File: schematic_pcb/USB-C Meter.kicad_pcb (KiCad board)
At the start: 4 copper layers, 51.5 x 45 mm, 68 parts, among them J1 USB-C 12P, J2 USB-C 12P, J3 Generic IN, J4 Generic OUT, J5 USB_B_Micro, J6 Display, J7 U.FL, J8 UART, U1 MP4560DN, U2 ME6211C33, U3 TPS2115, U4 ESP32-C3FH4, U6 INA228, Y1 40MHz

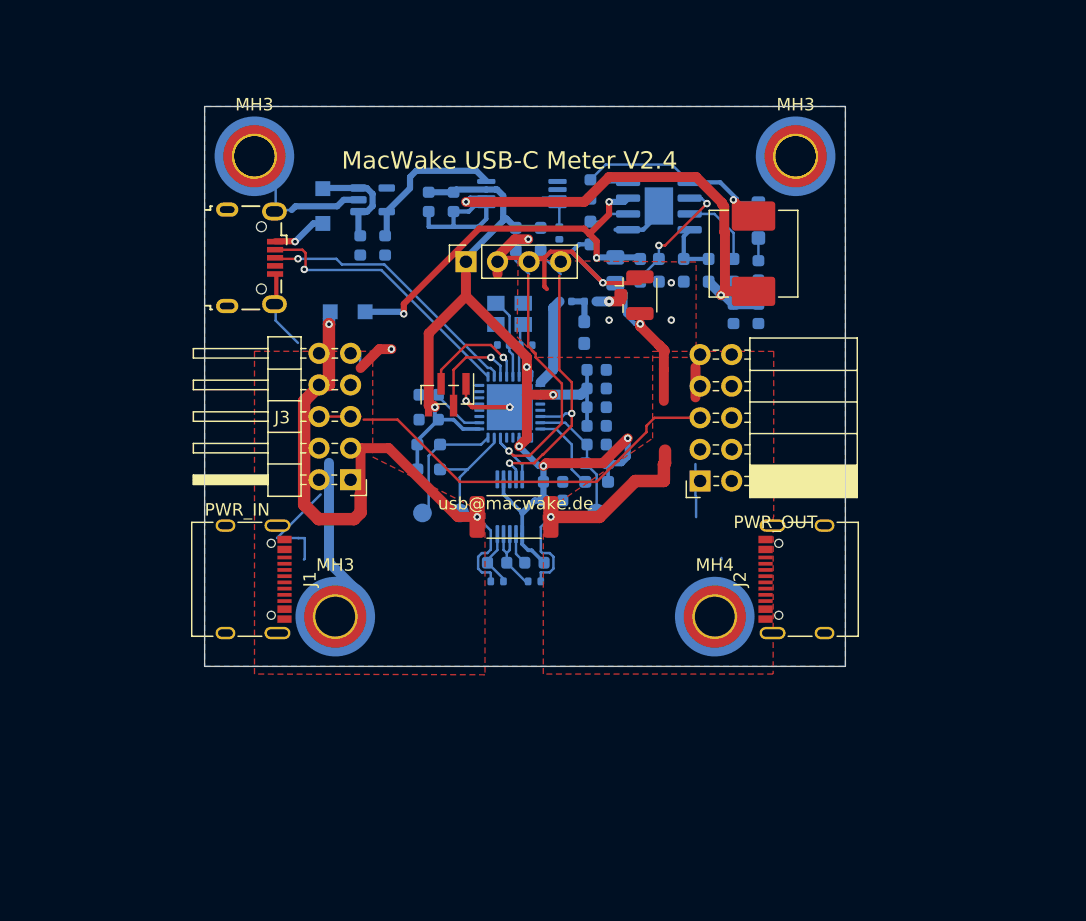
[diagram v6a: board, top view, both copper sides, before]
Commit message: fix: rf antenna pcb design, added reset tactile switch
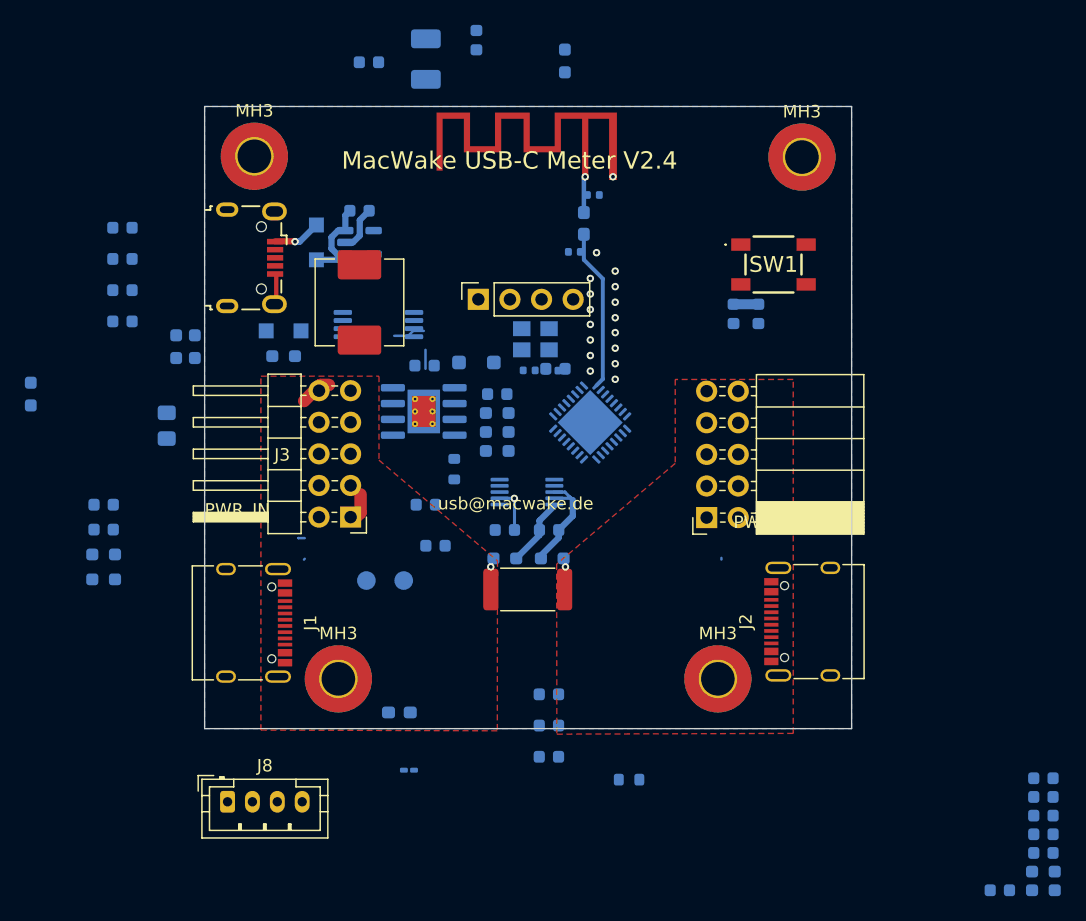
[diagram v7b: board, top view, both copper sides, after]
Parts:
- removed ? (x2): , 
- removed J7: U.FL, Connector_Coaxial:U.FL_Hirose_U.FL-R-SMT-1_Vertical
- removed MH4: MountingHole_3.2mm_M3_Pad_TopBottom, MountingHole:MountingHole_3.2mm_M3_Pad_TopBottom
- removed TP3: Reset, TestPoint:TestPoint_Pad_D1.5mm
- added AE1: Antenna_Shield, schematic_pcb:ESPRESSIF_ESP32_MIFA_2.4GHz_Right, F.Cu at (79.8, 30.6)
- added C2: 10µ, Capacitor_SMD:C_0603_1608Metric, B.Cu at (86.2, 72.2)
- added C27: .1µ, Capacitor_SMD:C_0603_1608Metric, B.Cu at (86.2, 77.3)
- added C28: .1µ, Capacitor_SMD:C_0603_1608Metric, B.Cu at (76.3, 57.0)
- added C29: 1µ, Capacitor_SMD:C_0603_1608Metric, B.Cu at (77.1, 60.3)
- added C3: 0.1µ, Capacitor_SMD:C_0603_1608Metric, B.Cu at (86.2, 74.8)
- added C30: .1µ, Capacitor_SMD:C_0603_1608Metric, B.Cu at (51.9, 37.3)
- added C31: .1µ, Capacitor_SMD:C_0603_1608Metric, B.Cu at (51.9, 39.8)
- added C32: .1µ, Capacitor_SMD:C_0603_1608Metric, B.Cu at (51.9, 42.3)
- added C33: 1µ, Capacitor_SMD:C_0603_1608Metric, B.Cu at (86.7, 46.1)
- added L3: 2nH, Inductor_SMD:L_0201_0603Metric_Pad0.64x0.40mm_HandSolder, B.Cu at (74.9, 78.3)
- added L4: 24nH, Inductor_SMD:L_0603_1608Metric_Pad1.05x0.95mm_HandSolder, B.Cu at (74.2, 73.7)
- added MH3: MountingHole_2.7mm_Pad_TopBottom, MountingHole:MountingHole_2.7mm_Pad_TopBottom, F.Cu at (99.8, 71.0)
- added R17: 500, Resistor_SMD:R_0603_1608Metric, B.Cu at (92.6, 79.1)
- added SW1: Reset, Project:PTS647SK70SMTR2LFS, F.Cu at (104.2, 37.7)
- C12: value 22µ -> 47µ; footprint Capacitor_SMD:C_0603_1608Metric -> Capacitor_Tantalum_SMD:CP_EIA-3528-12_Kemet-T_HandSolder
- C13: value 10µ -> 10µF
- C14: value 1µ -> .1µ
- C18, C21: value 0.1µ -> 1µ
- C24: value 1pF -> 1.5p
- C25: value 1pF -> 1.2p
- C4: value 4.7µ -> 10µ
- D1, D3: value CMMSH1-60G -> DS60_1
- J1, J2: value USB-C 12P -> USB-C Receptacle 16P
- J6: value Display -> Display I2C
- J8: footprint Connector_PinHeader_1.00mm:PinHeader_1x04_P1.00mm_Vertical_SMD_Pin1Left -> Connector_JST:JST_PH_B4B-PH-K_1x04_P2.00mm_Vertical
- L2: value 3.9nH -> 2.7nH
- MH3 (x3): value MountingHole_3.2mm_M3_Pad_TopBottom -> MountingHole_2.7mm_Pad_TopBottom; footprint MountingHole:MountingHole_3.2mm_M3_Pad_TopBottom -> MountingHole:MountingHole_2.7mm_Pad_TopBottom
- R10: value 400 -> 400R; footprint Resistor_SMD:R_0402_1005Metric -> Resistor_SMD:R_0603_1608Metric
- R14, R15, R16: value 12k -> 10k
- R2, R3: footprint Resistor_SMD:R_0402_1005Metric -> Resistor_SMD:R_0603_1608Metric_Pad0.98x0.95mm_HandSolder
- U1: footprint Package_SO:SOIC-8-1EP_3.9x4.9mm_P1.27mm_EP2.29x3mm -> Package_SO:SOIC-8-1EP_3.9x4.9mm_P1.27mm_EP2.62x3.51mm_ThermalVias
- moved C13 48.6 mm to (125.9, 82.0)
- moved C15 48.6 mm to (125.9, 83.5)
- moved C16 48.6 mm to (122.4, 88.0)
- moved C19 48.6 mm to (125.9, 80.5)
- moved C20 48.6 mm to (125.9, 79.0)
- moved C21 48.6 mm to (125.9, 85.0)
- moved R13 48.6 mm to (125.9, 88.0)
- moved R16 48.6 mm to (125.9, 86.5)
- moved C14 41.0 mm to (51.9, 34.7), turned to 180 degrees
- moved R12 40.9 mm to (44.5, 48.1)
- moved C4 38.2 mm to (55.5, 50.7)
- moved R4 37.8 mm to (56.2, 44.3)
- moved R5 37.8 mm to (57.7, 44.3)
- moved J8 37.2 mm to (60.3, 80.9), turned to 0 degrees
- moved L1 31.9 mm to (70.9, 40.7), turned to 90 degrees
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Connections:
- net Net-(C8-Pad1) renamed /MPCOMP_RC
- C14 pad 1: 3V3 -> /VBUS_PD_R
- C16 pad 1: GND -> 3V3
- C16 pad 2: 3V3 -> GND
- C17 pad 1: GND -> 3V3
- C17 pad 2: 3V3 -> GND
- C19 pad 2: 3V3 -> Net-(C19-Pad2)
- C20 pad 1: GND -> 3V3
- C20 pad 2: 3V3 -> GND
- C21 pad 1: GND -> Net-(U4-CHIP_EN)
- C21 pad 2: Net-(U4-CHIP_EN) -> GND
- C22 pad 2: Net-(U4-XTAL_P) -> Net-(C22-Pad2)
- C24 pad 1: /RF -> GND
- C24 pad 2: Net-(C24-Pad2) -> /RF
- C25 pad 2: Net-(C24-Pad2) -> GND
- J3 pad 5: /CHGR_ID_GENERIC -> /CHGR_ID_GENERIC_A
- J3 pad 6: /CHGR_ID_GENERIC -> /CHGR_ID_GENERIC_B
- J4 pad 5: /CHGR_ID_GENERIC -> /CHGR_ID_GENERIC_A
- J4 pad 6: /CHGR_ID_GENERIC -> /CHGR_ID_GENERIC_B
- J8 pad 1: GND -> 3V3
- J8 pad 4: 3V3 -> GND
- L2 pad 1: GND -> /RF
- L2 pad 2: Net-(C24-Pad2) -> /ANT
- MH3 pad 1: GND -> (no net)
- U4 pad 2: 3V3 -> Net-(C19-Pad2)
- U4 pad 27: Net-(J8-Pin_2) -> Net-(J8-Pin_3)
- U4 pad 28: Net-(J8-Pin_3) -> Net-(U4-U0TXD)
- U4 pad 3: 3V3 -> Net-(C19-Pad2)
- Y1 pad 3: Net-(U4-XTAL_P) -> Net-(C22-Pad2)
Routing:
- net GND: track 110.3 -> 6.74 mm, vias 9 -> 17
- net 3V3: track 97.0 -> 3.73 mm, vias 6 -> 1
- net /VBUS_PD_1_IN: track 45.4 -> 4.74 mm, vias 2 -> 1
- net /VBUS_PD_3V3: track 38.8 -> 2.00 mm, vias 2 -> 0
- net /CHGR_ID_GENERIC: track 33.7 -> 0.00 mm
- net /VBUS_PD_R: track 32.0 -> 0.00 mm, vias 3 -> 0
- net /VBUS_PD_2_IN: track 26.4 -> 0.00 mm
- net SCL: track 25.9 -> 0.00 mm, vias 1 -> 0
- net SDA: track 25.2 -> 0.00 mm, vias 2 -> 0
- net /D-: track 22.3 -> 0.00 mm, vias 1 -> 0
- net /D+: track 21.7 -> 0.00 mm, vias 1 -> 0
- net Net-(D2-K): track 18.0 -> 0.00 mm, vias 1 -> 0
- net /VBUS_DATA_3V3: track 12.0 -> 0.00 mm
- net Net-(U4-CHIP_EN): track 10.2 -> 0.00 mm
- net Net-(U4-GPIO10): track 10.2 -> 0.00 mm
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- added copper zone on In2.Cu, net 3V3
- removed copper zone on F.Cu, net GND
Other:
- board size 51.5 x 45 mm -> 52 x 50 mm

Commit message: feat: reroute antenna and all other components
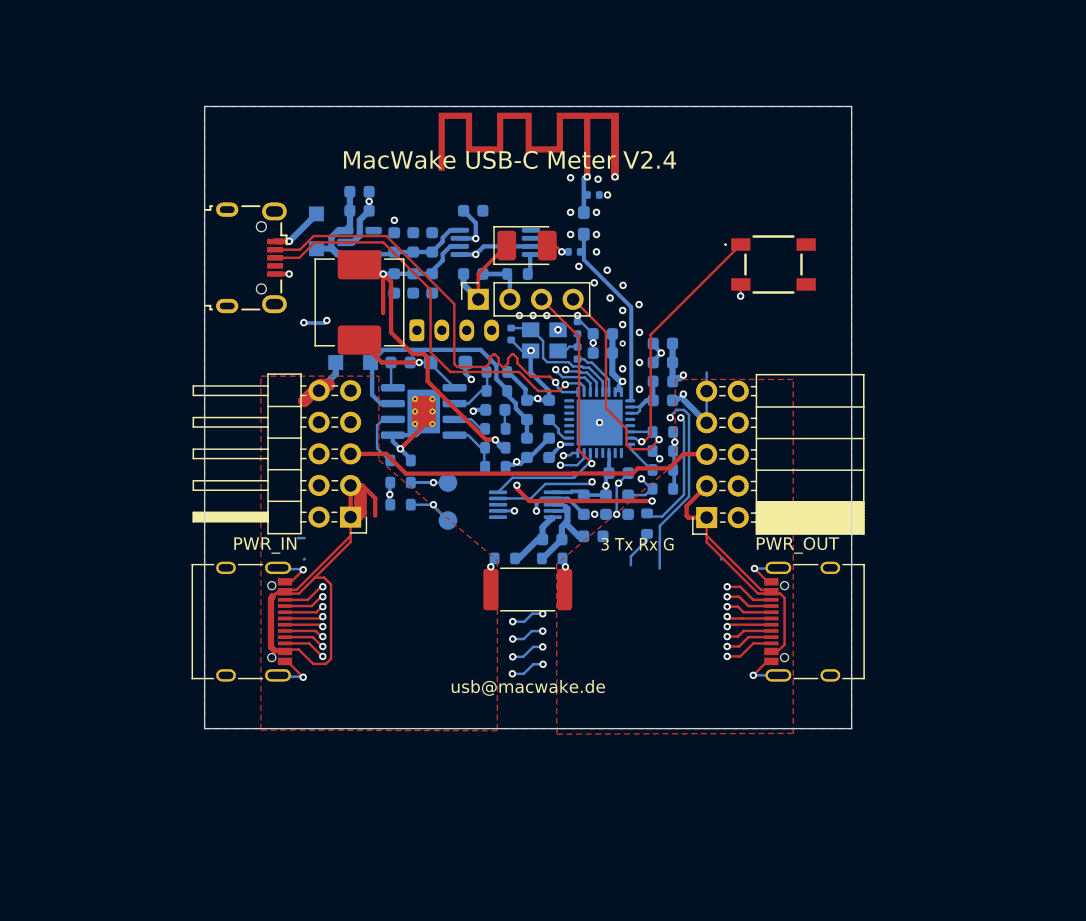
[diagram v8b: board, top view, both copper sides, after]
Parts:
- removed C28: .1µ, Capacitor_SMD:C_0603_1608Metric
- removed MH3 (x4): MountingHole_2.7mm_Pad_TopBottom, MountingHole:MountingHole_2.7mm_Pad_TopBottom
- C12: moved to F.Cu
- C4: footprint Capacitor_SMD:C_0805_2012Metric_Pad1.18x1.45mm_HandSolder -> Capacitor_SMD:C_0603_1608Metric
- J6: value Display I2C -> Display
- L3: footprint Inductor_SMD:L_0201_0603Metric_Pad0.64x0.40mm_HandSolder -> Inductor_SMD:L_0603_1608Metric
- L4: footprint Inductor_SMD:L_0603_1608Metric_Pad1.05x0.95mm_HandSolder -> Inductor_SMD:L_0402_1005Metric
- R11, R12, R13, R14, R15, R16, R2, R3, R4, R5, R6, R7, R8, R9: footprint Resistor_SMD:R_0603_1608Metric_Pad0.98x0.95mm_HandSolder -> Resistor_SMD:R_0603_1608Metric
- moved R12 51.0 mm to (95.3, 52.7), turned to 0 degrees
- moved C20 49.2 mm to (90.5, 44.8)
- moved C13 48.7 mm to (95.3, 44.0), turned to 180 degrees
- moved C15 48.7 mm to (95.3, 45.6), turned to 180 degrees
- moved R13 45.6 mm to (95.3, 54.2)
- moved C16 45.4 mm to (91.8, 54.5), turned to 0 degrees
- moved C27 44.3 mm to (80.1, 33.4), turned to 0 degrees
- moved C19 44.2 mm to (95.3, 48.6)
- moved C21 43.6 mm to (92.5, 57.0), turned to -90 degrees
- moved R16 43.4 mm to (95.3, 55.7)
- moved J8 40.8 mm to (75.6, 43.0)
- moved L3 37.3 mm to (95.3, 47.1)
- moved C18 36.6 mm to (86.2, 49.4), turned to -90 degrees
- moved C17 36.4 mm to (86.2, 52.4), turned to 90 degrees
- moved C14 35.7 mm to (84.4, 49.4), turned to 90 degrees
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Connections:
- net Net-(C19-Pad2) renamed /3V3_FLT
- net Net-(U4-GPIO10) renamed /EXP
- net Net-(U4-GPIO9) renamed /BOOT
- net Net-(U4-U0TXD) renamed /UTXD
- J2 pad A5: /CC1 -> /CC2
- J2 pad A6: Net-(J1-D+-PadA6) -> Net-(J1-D+-PadB6)
- J2 pad A7: Net-(J1-D--PadA7) -> Net-(J1-D--PadB7)
- J2 pad A8: Net-(J1-SBU1) -> Net-(J1-SBU2)
- J2 pad B5: /CC2 -> /CC1
- J2 pad B6: Net-(J1-D+-PadB6) -> Net-(J1-D+-PadA6)
- J2 pad B7: Net-(J1-D--PadB7) -> Net-(J1-D--PadA7)
- J2 pad B8: Net-(J1-SBU2) -> Net-(J1-SBU1)
- J8 pad 1: 3V3 -> (no net)
- J8 pad 2: Net-(J8-Pin_2) -> (no net)
- J8 pad 3: Net-(J8-Pin_3) -> (no net)
- J8 pad 4: GND -> (no net)
- R17 pad 1: Net-(J8-Pin_2) -> /UTXD_F
- U4 pad 27: Net-(J8-Pin_3) -> /URXD
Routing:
- net GND: track 6.74 -> 96.7 mm, vias 17 -> 51
- net /VBUS_PD_1_IN: track 4.74 -> 49.9 mm
- net Net-(J1-SBU2): track 0.00 -> 41.9 mm, vias 0 -> 2
- net /CC1: track 0.00 -> 41.8 mm, vias 0 -> 4
- net Net-(J1-SBU1): track 0.00 -> 41.3 mm, vias 0 -> 2
- net /CC2: track 0.00 -> 41.3 mm, vias 0 -> 4
- net Net-(J1-D+-PadA6): track 0.00 -> 41.1 mm, vias 0 -> 4
- net Net-(J1-D--PadB7): track 0.00 -> 41.1 mm, vias 0 -> 2
- net Net-(J1-D--PadA7): track 0.00 -> 41.1 mm, vias 0 -> 2
- net Net-(J1-D+-PadB6): track 0.00 -> 41.0 mm, vias 0 -> 4
- net 3V3: track 3.73 -> 42.2 mm, vias 1 -> 10
- net /CHGR_ID_GENERIC_B: track 0.00 -> 37.6 mm, vias 0 -> 2
- net SDA: track 0.00 -> 36.3 mm, vias 0 -> 2
- net /D-: track 0.00 -> 35.6 mm, vias 0 -> 1
- net SCL: track 0.00 -> 34.4 mm, vias 0 -> 2
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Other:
- board text added: "3 Tx Rx G"
